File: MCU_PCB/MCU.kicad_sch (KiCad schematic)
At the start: 16 parts, among them J1 Conn_01x06_Socket, J2 Conn_01x06_Socket, J5 Conn_01x02_Pin, M1 MountingHole, M3_1 MountingHole, M3_2 MountingHole, U1 ESP32-DEVKIT-C, U2 TJA1050T/CM,118

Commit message: updated Julias IMU to use the revised buck converter and connectors. made the back plane mostly a ground plane (for the buck converter)
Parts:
- renumbered J1 to J3, U1 to U3
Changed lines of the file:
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@@
 		(dnp no)
 		(fields_autoplaced yes)
-		(property "Reference" "J1"
+		(property "Reference" "J3"
 			(at 27.94 107.95 0)
 			(show_name no)
@@
 			(project "MCU"
 				(path "/c58806c5-432f-4c41-8983-8e5fd30a3703"
-					(reference "J1")
+					(reference "J3")
 					(unit 1)
 				)
@@
 		(dnp no)
 		(fields_autoplaced yes)
-		(property "Reference" "U1"
+		(property "Reference" "U3"
 			(at 120.65 101.6 0)
 			(show_name no)
@@
 			(project "MCU"
 				(path "/c58806c5-432f-4c41-8983-8e5fd30a3703"
-					(reference "U1")
+					(reference "U3")
 					(unit 1)
 				)

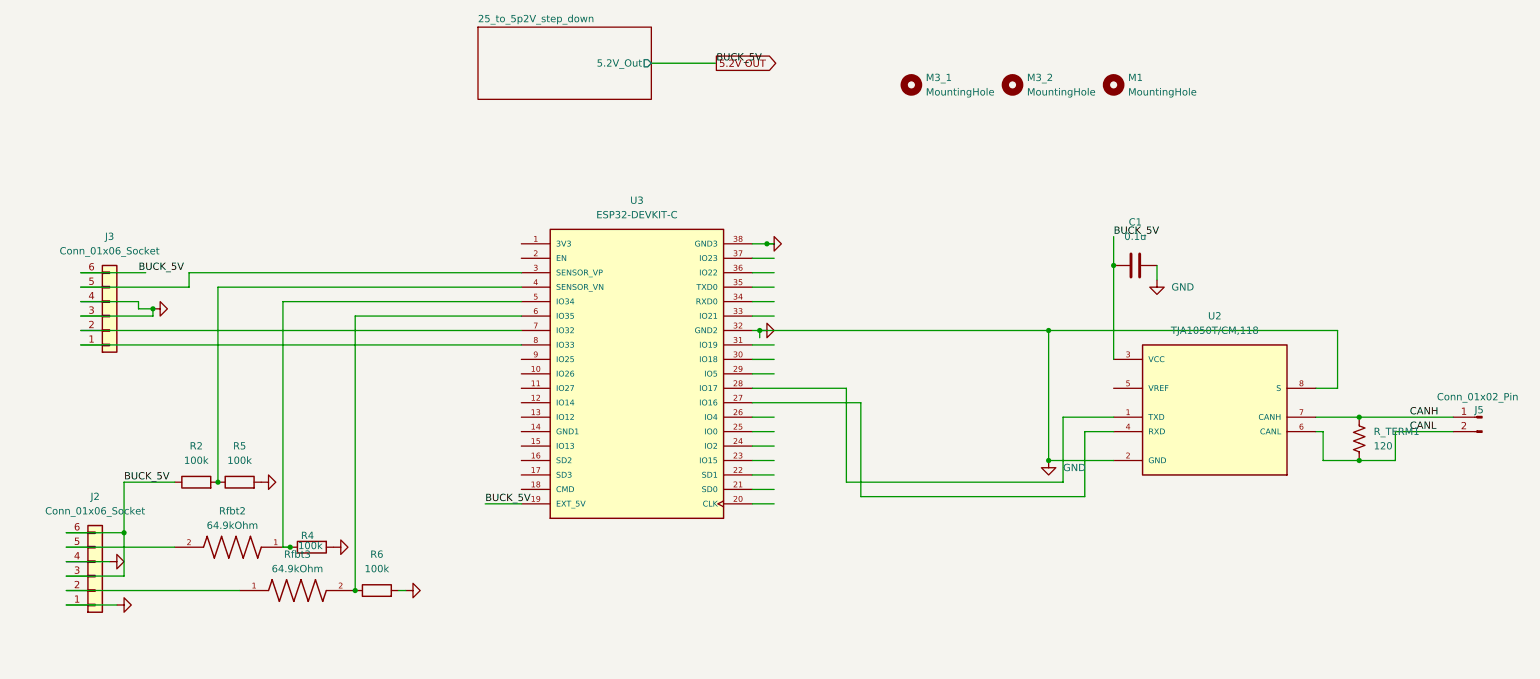
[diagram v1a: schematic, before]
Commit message: sry forgot to push, waiting on PCB shipping atm. Notes: split power distribution into two boards, one for the main 25V distribution, and another for 12V stuff. Also updated CAN transciever. the previous one was a 5V logic one (same logic as its power), and would have fried our ESPs data pins
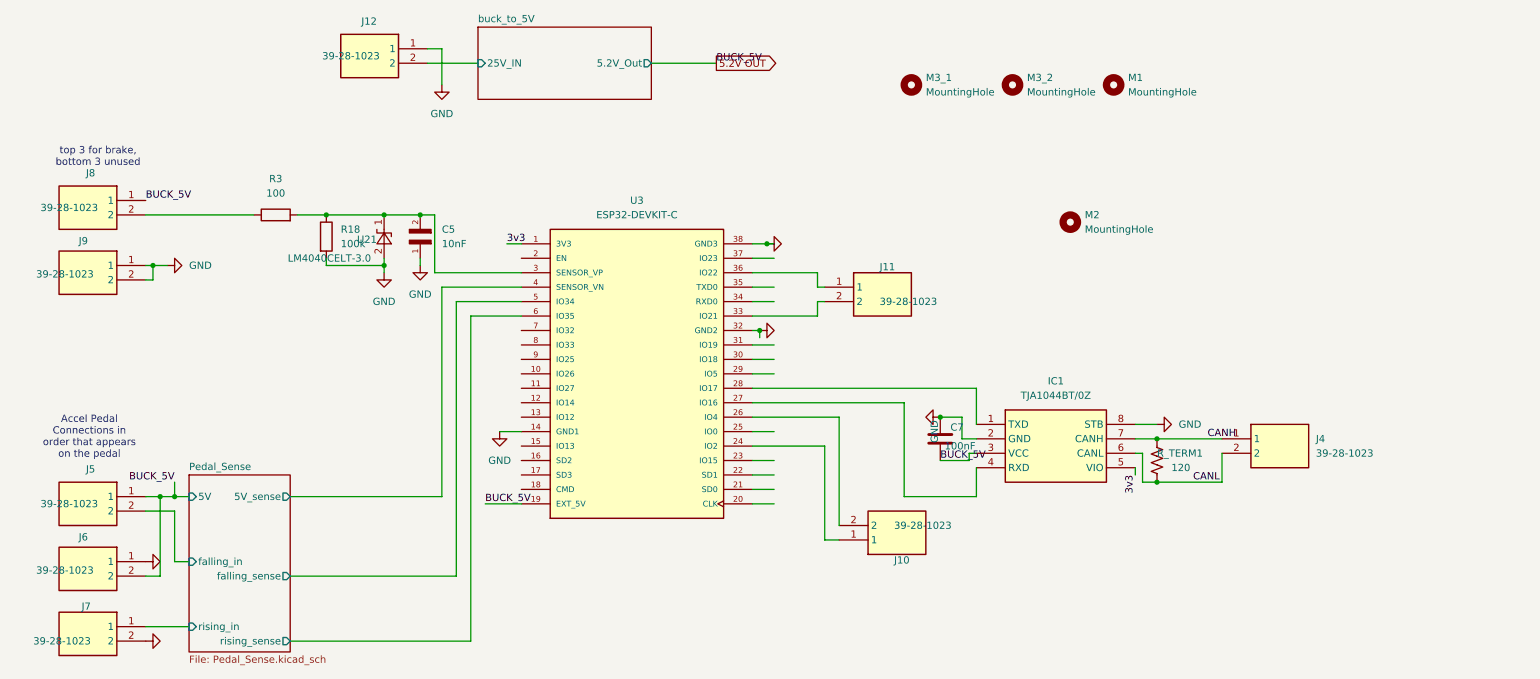
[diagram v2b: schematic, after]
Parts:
- removed C1: 0.1u, Capacitor_SMD:C_1206_3216Metric_Pad1.33x1.80mm_HandSolder, symbol PROVE:1206B104K500CT
- removed J2, J3: Conn_01x06_Socket, PROVE-footprints:TE_1877285-6, symbol Connector_Generic:Conn_01x06
- removed J5: Conn_01x02_Pin, PROVE-footprints:TE_1877285-2, symbol Connector:Conn_01x02_Pin
- removed R2, R4, R5, R6: 100k, Resistor_SMD:R_1206_3216Metric_Pad1.30x1.75mm_HandSolder, symbol Device:R
- removed Rfbt2, Rfbt3: 64.9kOhm, Resistor_SMD:R_1206_3216Metric_Pad1.30x1.75mm_HandSolder, symbol CRCW040211K0FKED:CRCW040211K0FKED
- removed U2: TJA1050T/CM,118, Package_SO:SOIC-8_3.9x4.9mm_P1.27mm, symbol PROVE:TJA1050T/CM,118
- added C5: 10nF, Capacitor_SMD:C_0805_2012Metric_Pad1.18x1.45mm_HandSolder, symbol C0805C122J5GACTU:C0805C122J5GACTU
- added C7: 100nF, Capacitor_SMD:C_0805_2012Metric_Pad1.18x1.45mm_HandSolder, symbol PROVE:1206B104K500CT
- added IC1: TJA1044BT/0Z, PROVE-footprints:SOIC127P600X175-8N, symbol PROVE_Symbols:TJA1044BT_0Z
- added J10, J11, J12, J4, J5, J6, J7, J8, J9: 39-28-1023, PROVE-footprints:39-28-1023, symbol PROVE_Symbols:39-28-1023
- added M2: MountingHole, MountingHole:MountingHole_3.2mm_M3, symbol Mechanical:MountingHole
- added R18: 100k, Resistor_SMD:R_0805_2012Metric_Pad1.20x1.40mm_HandSolder, symbol Device:R
- added R3: 100, Resistor_SMD:R_0805_2012Metric_Pad1.20x1.40mm_HandSolder, symbol Device:R
- added U21: LM4040CELT-3.0, Package_TO_SOT_SMD:SOT-23, symbol Reference_Voltage:LM4040DBZ-3
- R_TERM1: footprint Resistor_SMD:R_1206_3216Metric_Pad1.30x1.75mm_HandSolder -> Resistor_SMD:R_0805_2012Metric_Pad1.20x1.40mm_HandSolder; Purchase Link (none) -> https://www.mouser.com/en/ProductDetail/Vishay/CRCW0805120R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; Specs (none) -> 120 Ω, ±1%, AEC-Q200,
- U3: MANUFACTURER ESPRESSIF -> (none)
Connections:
- net 5.2V OUT: now also C7.1, IC1.3 (VCC), J5.1, J6.2, J8.1
- net CANH: now also IC1.7 (CANH), J4.1
- net CANL: now also IC1.6 (CANL), J4.2
- net GND: now also U3.14 (GND1), C5.1, C7.2, IC1.2 (GND), IC1.8 (STB), J12.1, J6.1, J7.2, J9.1, J9.2, R18.2, U21.2 (A)
- net Pedal_Sense/falling_sense: now reaches U3.5 (IO34)
- net at U3.28 (IO17): now also IC1.1 (TXD)
- net at U3.27 (IO16): now also IC1.4 (RXD)
- net Pedal_Sense/rising_sense: now reaches U3.6 (IO35)
- net Pedal_Sense/5V_sense: now reaches U3.4 (SENSOR_VN)
- net at U3.3 (SENSOR_VP): now also C5.2, R18.1, R3.2, U21.1 (K)
- net 3v3: now reaches U3.1 (3V3)
- net 3v3: now also IC1.5 (VIO)
- net at U3.24 (IO2): now also J10.1
- net at U3.26 (IO4): now also J10.2
- net at U3.33 (IO21): now also J11.2
- net at U3.36 (IO22): now also J11.1
- new net: J8.2, R3.1
- new net Pedal_Sense/falling_in: J5.2
- new net Pedal_Sense/rising_in: J7.1
- new net buck_to_5V/25V_IN: J12.2
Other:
- sheet 25_to_5p2V_step_down renamed buck_to_5V
- added sheet Pedal_Sense (Pedal_Sense.kicad_sch)
- sheet buck_to_5V: file ../buck_converter.kicad_blocks/25_to_5p2V_step_down.kicad_block/25_to_5p2V_step_down.kicad_sch -> ../buck_converter.kicad_blocks/buck_to_5V.kicad_block/buck_to_5V.kicad_sch
- sheet buck_to_5V ports: added 25V_IN; removed none
- note added: "Accel Pedal Connections in order that appears on the pedal"
- note added: "top 3 for brake, bottom 3 unused"
